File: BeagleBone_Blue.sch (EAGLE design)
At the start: 417 parts, among them J1 68000-406HLF, M1 JST_ZH_2, M2 JST_ZH_2, M3 JST_ZH_2, M4 JST_ZH_2, P10 SCHA5B0200, P2 CTIJTAG, P3 87520-0010BLF, P4 UX60SC-MB-5ST(80), Q3 MOSFET-N, Q4 MOSFET-P, U1 MPU-9250, U10 TPD4S012, U12 MT41K256M16HA, U13 MTFC4GLDEA, U15 SN74LVC2G241DCU, U16 SN74LVC1G07DCK, U3 SN74LVC1G06DCK, U4 TL5209, U5 AM3358_BZCZ_324, U6 SN74LVC1G74_DCT_8, U7 24LC_32AT-I/OT, U8 TPS2051BD, U9 TPD4S012, Y1 CM200C-32.768KAZF-UT, Y2 445C33D24M00000, Y4 ASDMB-24.576MHZ-LC-T

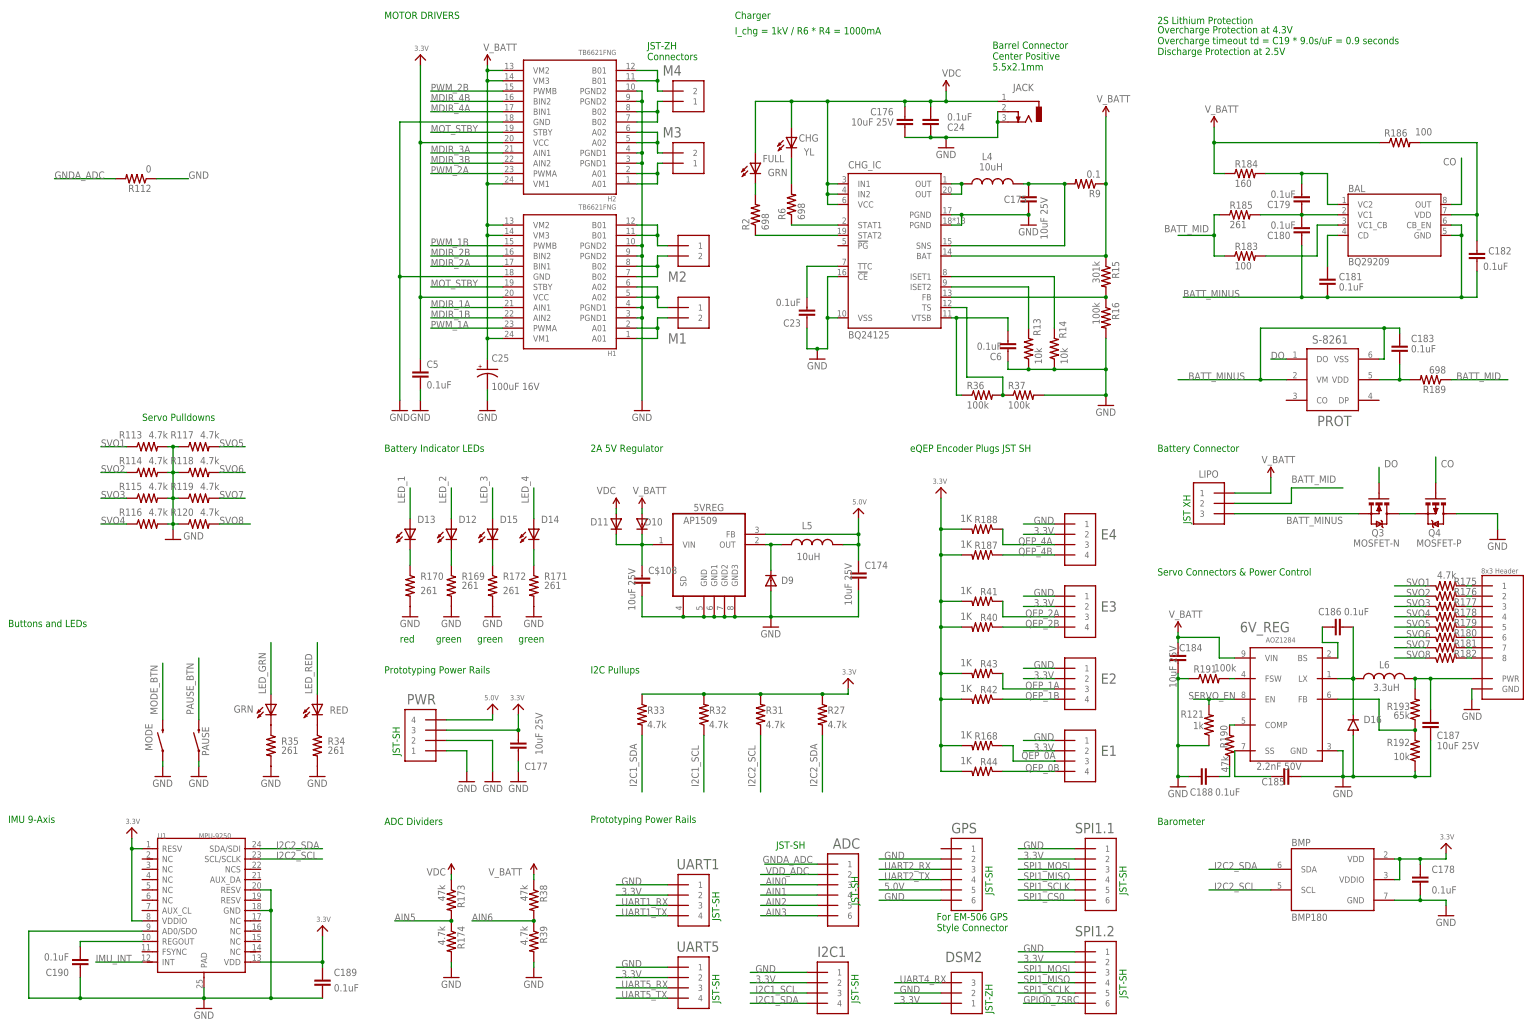
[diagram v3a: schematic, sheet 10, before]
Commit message: Merge new charger to Blue schematic
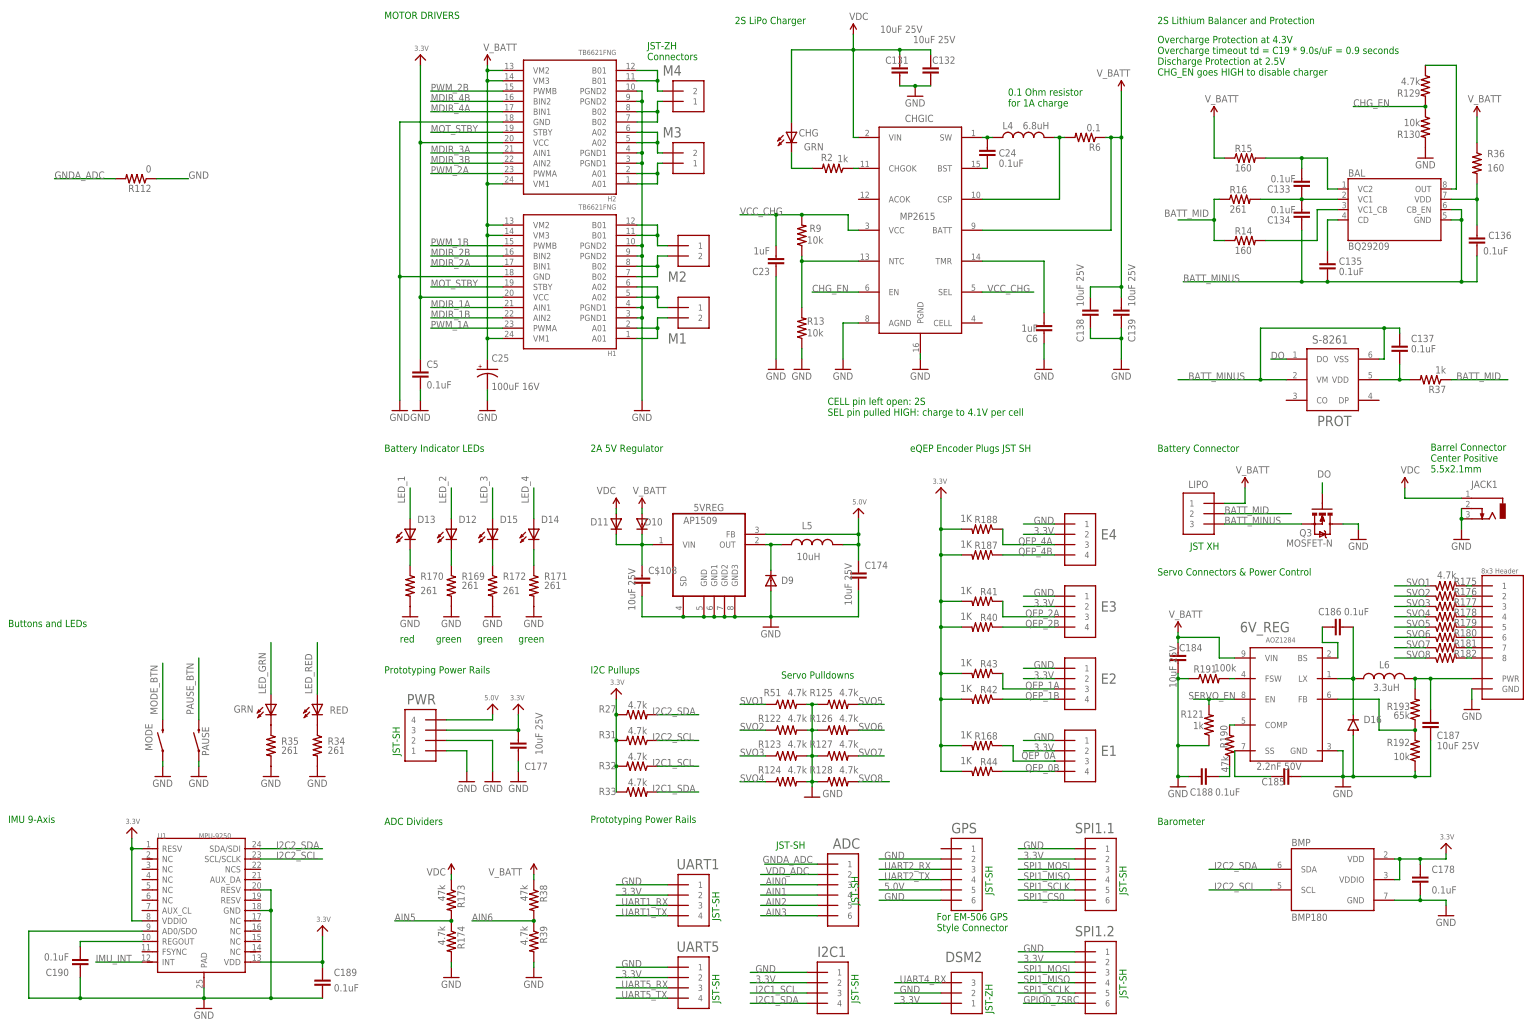
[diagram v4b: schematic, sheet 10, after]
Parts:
- removed C175, C176: 10uF 25V, SparkFun-Capacitors:CAP0805
- removed C179, C180, C181, C182: 0.1uF, Strawson_Eagle_Lib:CAP0402-CAP
- removed CHG_IC: BQ24125, Strawson_Eagle_Lib:BQ24125
- removed FULL: GRN, SparkFun-LED:LED0603
- removed JACK: 5.5x2.1mm, con-jack:DCJ0303
- removed Q4: MOSFET-P, Strawson_Eagle_Lib:MOSFET-PCHANNEL
- removed R113, R114, R115, R116, R117, R118, R119, R120: 4.7k, Strawson_Eagle_Lib:RESISTOR0402-RES
- removed R183, R186: 100, Strawson_Eagle_Lib:RESISTOR0402-RES
- removed R184: 160, Strawson_Eagle_Lib:RESISTOR0402-RES
- removed R185: 261, Strawson_Eagle_Lib:RESISTOR0402-RES
- removed R189: 698, Strawson_Eagle_Lib:RESISTOR0402-RES
- added C131, C132, C138, C139: 10uF 25V, SparkFun-Capacitors:CAP0805
- added C133, C134, C135, C136: 0.1uF, Strawson_Eagle_Lib:CAP0402-CAP
- added CHGIC: MP2615, Strawson_Eagle_Lib:MP2615
- added JACK1: 5.5x2.1mm, con-jack:DCJ0303
- added R122, R123, R124, R125, R126, R127, R128, R129, R51: 4.7k, Strawson_Eagle_Lib:RESISTOR0402-RES
- added R130: 10k, Strawson_Eagle_Lib:RESISTOR0402-RES
- C23, C6: value 0.1uF -> 1uF
- CHG: value YL -> GRN
- L4: value 10uH -> 6.8uH
- R14: value 10k -> 160
- R15: value 301k -> 160
- R16: value 100k -> 261
- R2: value 698 -> 1k
- R36: value 100k -> 160
- R37: value 100k -> 1k
- R6: value 698 -> 0.1; device Strawson_Eagle_Lib:RESISTOR0402-RES -> SparkFun-Resistors:RESISTOR0603
- R9: value 0.1 -> 10k; device SparkFun-Resistors:RESISTOR0603 -> Strawson_Eagle_Lib:RESISTOR0402-RES
- renumbered C183 to C137
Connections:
- removed net N$23: CHG_IC.STAT2, R2.1
- removed net N$26: BAL.CD, C181.1
- removed net N$27: C137.2, PROT.VDD, R189.2
- removed net N$28: C6.2, CHG_IC.VTSB, R36.1
- removed net N$31: CHG_IC.TS, R36.2, R37.1
- removed net N$32: Q3.D, Q4.S
- removed net N$35: CHG_IC.ISET2, R13.2
- removed net N$36: CHG_IC.FB, R15.2, R16.1
- removed net N$37: CHG_IC.ISET1, R14.2
- removed net N$46: C23.2, CHG_IC.TTC
- new net CHG_EN: CHGIC.EN, R129.2, R130.1
- new net N$4: CHG.C, R2.2
- new net N$55: C24.2, CHGIC.SW, L4.1
- new net N$67: CHGIC.CSP, L4.2, R6.2
- new net N$69: C6.2, CHGIC.TMR
- new net VCC_CHG: C23.2, CHGIC.SEL, CHGIC.VCC, R9.2
- net BATT_MID: now also R14.1, R16.1, R37.1; no longer R183.1, R185.1, R189.1
- net BATT_MINUS: now also C134.1, C135.2, C136.2; no longer C180.1, C181.2, C182.2
- net CO: now also R129.1; no longer Q4.G
- net GND: now also C131.2, C132.2, C138.2, C139.2, CHGIC.AGND, CHGIC.PGND, JACK1.2, JACK1.3, Q3.D, R122.2, R123.2, R124.2, R125.1, R126.1, R127.1, R128.1, R130.2, R51.2; no longer C175.2, C176.2, C24.1, CHG_IC.!CE, CHG_IC.PGND@1, CHG_IC.PGND@2, CHG_IC.VSS, JACK.2, JACK.3, Q4.D, R113.2, R114.2, R115.2, R116.2, R117.1, R118.1, R119.1, R120.1, R14.1, R16.2, R37.2
- net N$13: now also C137.2, PROT.VDD, R37.2; no longer CHG_IC.OUT@1, CHG_IC.OUT@2, L4.1
- net N$14: now also C24.1, CHGIC.BST; no longer C175.1, CHG_IC.SNS, L4.2, R9.2
- net N$18: now also CHGIC.CHGOK, R2.1; no longer CHG_IC.STAT1, R6.1
- net N$21: now also CHGIC.NTC, R13.2, R9.1; no longer BAL.VC1, C179.1, C180.2, R185.2
- net N$24: now also BAL.CD, C135.1; no longer BAL.VC2, C179.2, R184.2
- net N$29: now also C136.1, R36.2; no longer C182.1, R186.2
- net N$50: now also R14.2; no longer R183.2
- net N$6: now also BAL.VC1, C133.1, C134.2, R16.2; no longer FULL.C, R2.2
- net N$7: now also BAL.VC2, C133.2, R15.2; no longer CHG.C, R6.2
- net SVO1: now also R51.1; no longer R113.1
- net SVO2: now also R122.1; no longer R114.1
- net SVO3: now also R123.1; no longer R115.1
- net SVO4: now also R124.1; no longer R116.1
- net SVO5: now also R125.2; no longer R117.2
- net SVO6: now also R126.2; no longer R118.2
- net SVO7: now also R127.2; no longer R119.2
- net SVO8: now also R128.2; no longer R120.2
- net VCC: now also C131.1, C132.1, CHGIC.VIN, JACK1.1; no longer C176.1, C24.2, CHG_IC.IN1, CHG_IC.IN2, CHG_IC.VCC, FULL.A, JACK.1
- net V_BATT: now also C138.1, C139.1, CHGIC.BATT, R36.1, R6.1; no longer CHG_IC.BAT, R184.1, R186.1, R9.1
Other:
- note added: "0.1 Ohm resistor for 1A charge"
- note added: "2S LiPo Charger"
- note added: "2S Lithium Balancer and Protection"
- note added: "CELL pin left open: 2S SEL pin pulled HIGH: charge to 4.1V per cell"
- note added: "Overcharge Protection at 4.3V Overcharge timeout td = C19 * 9.0s/uF = 0.9 seconds Discharge Protection at 2.5V CHG_EN goes HIGH to disable charger"
- note removed: "2S Lithium Protection"
- note removed: "Charger"
- note removed: "I_chg = 1kV / R6 * R4 = 1000mA"
- note removed: "Overcharge Protection at 4.3V Overcharge timeout td = C19 * 9.0s/uF = 0.9 seconds Discharge Protection at 2.5V"
- moved on the sheet: BAL, C23, C24, C6, CHG, L4, LIPO, Q3, R13, R14, R15, R16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

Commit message: Remove SD card slot and Label SDIO&UART5 for WIFi use on page 9
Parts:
- removed P10: SCHA5B0200, SCHA5B0200:SCHA5B0200
- removed UART5: JST_SH_4, Strawson_Eagle_Lib:JST_SH_4
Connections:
- net 3.3V: no longer UART5.2
- net GND: no longer P10.GND, P10.GND3, P10.GND4, P10.GND5, P10.GND6, P10.GND7, P10.GND8, P10.VSS, UART5.1
- net MMC0_CD: no longer P10.CD
- net MMC0_CLK0: no longer P10.CLOCK
- net MMC0_CMD: no longer P10.CMD
- net MMC0_DAT0: no longer P10.DAT0
- net MMC0_DAT1: no longer P10.DAT1
- net MMC0_DAT2: no longer P10.DAT2
- net MMC0_DAT3: no longer P10.CD/DAT3
- net UART5_RX: no longer UART5.3
- net UART5_TX: no longer UART5.4
- net VCC: no longer P10.VDD
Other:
- note added: "SDIO lines for WiFi Module"
- note added: "UART interface for WiFi Module"
- note removed: "uSD CONNECTOR"
- moved on the sheet: C152, C153, C154, R150, R151, R152, R153, R154, R155, R156, R157, U7

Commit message: reserve last gpio pins for WIFI_EN and BT_EN
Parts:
- added UART5: JST_SH_4, Strawson_Eagle_Lib:JST_SH_4
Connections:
- net GPIO1_17 renamed WIFI_EN
- net N$226 renamed UART0_RX
- net N$227 renamed UART0_TX
- new net BT_EN: U5G$2.MCASP0_AXR1/EQEP0_INDEX//MCASP1_AXR0/EMU3/PR1_PRU0_PRU_R30_6/PR1_PRU0_PRU_R31_6/GPIO3_20
- net 3.3V: now also UART5.2
- net GND: now also UART5.1
- net GPIO3_20: no longer U5G$2.MCASP0_AXR1/EQEP0_INDEX//MCASP1_AXR0/EMU3/PR1_PRU0_PRU_R30_6/PR1_PRU0_PRU_R31_6/GPIO3_20
- net UART5_RX: now also UART5.3
- net UART5_TX: now also UART5.4
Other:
- note added: "UART0 for WiLink8 NOTE: also used for debug header"
- note removed: "UART interface for WiFi Module"
- note removed: "UART0_RX"
- note removed: "UART0_TX"

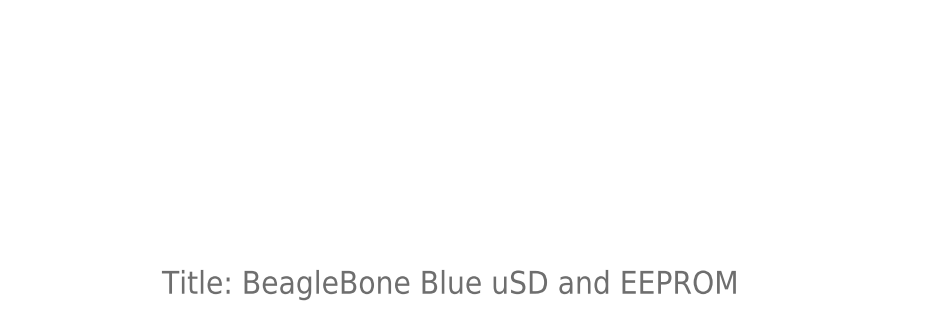
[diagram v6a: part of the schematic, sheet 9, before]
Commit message: dedicate page 9 to WiFi BT Module
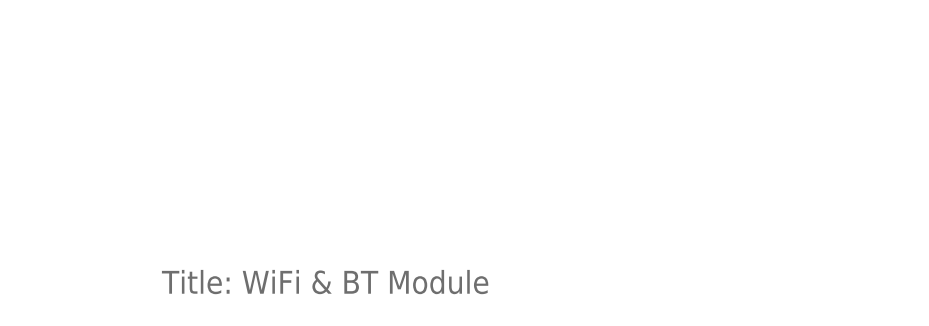
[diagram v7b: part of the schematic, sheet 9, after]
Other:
- note added: "Title: WiFi & BT Module"
- note removed: "Title: BeagleBone Blue uSD and EEPROM"
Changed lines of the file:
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@@
 <sheet>
 <plain>
-<text x="477.52" y="35.56" size="2.54" layer="95">Title: BeagleBone Blue uSD and EEPROM</text>
+<text x="477.52" y="35.56" size="2.54" layer="95">Title: WiFi &amp; BT Module</text>
 <text x="109.22" y="304.8" size="1.778" layer="96" rot="R90">10K,1%</text>
 <text x="114.3" y="304.8" size="1.778" layer="96" rot="R90">10K,1%</text>
